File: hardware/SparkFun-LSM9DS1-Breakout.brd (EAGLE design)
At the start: 22.9 x 22.9 mm, 27 parts, among them U1 LSM9DS1

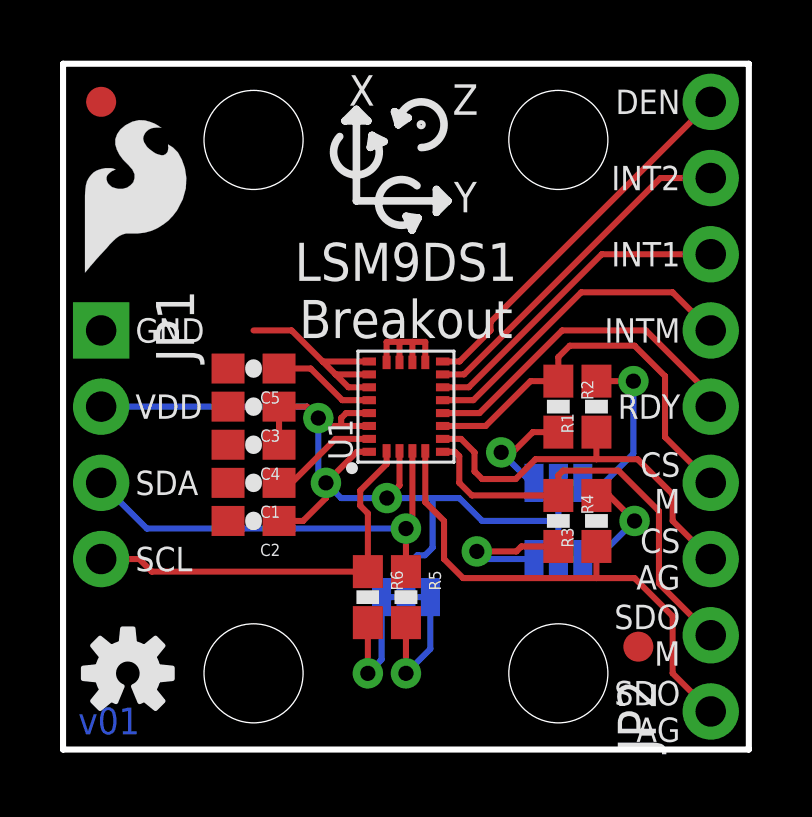
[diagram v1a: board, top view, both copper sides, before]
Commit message: Adding board mesurements, fixing some traces, labelling VCC range.
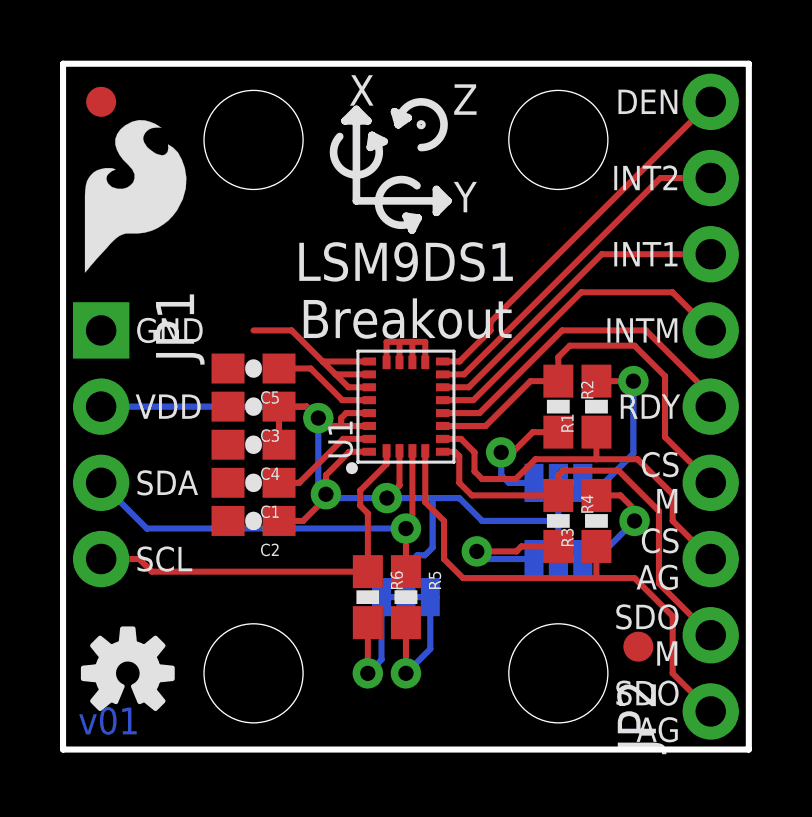
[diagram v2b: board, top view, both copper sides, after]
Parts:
- moved FRAME1 12.7 mm to (-15.2, -22.9)
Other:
- board text added: "1.9-3.6V"
- board text added: "Units in inches"
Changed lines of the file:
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@@
 <setting verticaltext="up"/>
 </settings>
-<grid distance="0.05" unitdist="inch" unit="inch" style="lines" multiple="1" display="yes" altdistance="0.005" altunitdist="inch" altunit="inch"/>
+<grid distance="0.05" unitdist="inch" unit="inch" style="lines" multiple="1" display="yes" altdistance="0.0025" altunitdist="inch" altunit="inch"/>
 <layers>
 <layer number="1" name="Top" color="4" fill="1" visible="yes" active="yes"/>
@@
 <layer number="47" name="Measures" color="7" fill="1" visible="no" active="yes"/>
 <layer number="48" name="Document" color="7" fill="1" visible="no" active="yes"/>
-<layer number="49" name="Reference" color="7" fill="1" visible="no" active="yes"/>
+<layer number="49" name="Reference" color="7" fill="1" visible="yes" active="yes"/>
 <layer number="50" name="dxf" color="7" fill="1" visible="no" active="no"/>
 <layer number="51" name="tDocu" color="6" fill="1" visible="yes" active="yes"/>
@@
 <text x="20.574" y="11.43" size="0.8128" layer="21" font="vector" ratio="15" align="center-right">RDY</text>
 <text x="2.286" y="13.97" size="0.8128" layer="22" font="vector" ratio="15" rot="MR0" align="center-right">GND</text>
-<text x="2.286" y="11.43" size="0.8128" layer="22" font="vector" ratio="15" rot="MR0" align="center-right">VDD</text>
+<text x="2.286" y="11.43" size="0.8128" layer="22" font="vector" ratio="15" rot="MR0" align="center-right">1.9-3.6V</text>
 <text x="2.286" y="8.89" size="0.8128" layer="22" font="vector" ratio="15" rot="MR0" align="center-right">SDA</text>
 <text x="2.286" y="6.35" size="0.8128" layer="22" font="vector" ratio="15" rot="MR0" align="center-right">SCL</text>
@@
 <text x="17.272" y="10.033" size="0.8128" layer="22" font="vector" ratio="15" rot="MR0" align="bottom-center">AG</text>
 <text x="9.398" y="4.699" size="0.8128" layer="22" font="vector" ratio="15" rot="MR0" align="bottom-center">I</text>
-<text x="7.366" y="4.699" size="0.8128" layer="22" font="vector" ratio="15" rot="MR0" align="bottom-center">C PU</text>
-<text x="9.017" y="5.334" size="0.635" layer="22" font="vector" ratio="15" rot="MR0" align="bottom-center">2</text>
+<text x="7.239" y="4.699" size="0.8128" layer="22" font="vector" ratio="15" rot="MR0" align="bottom-center">C PU</text>
+<text x="8.9535" y="5.2705" size="0.635" layer="22" font="vector" ratio="15" rot="MR0" align="bottom-center">2</text>
 <text x="13.0556" y="17.9324" size="0.8128" layer="22" font="vector" ratio="15" rot="MR0" align="center">SDO
 0
@@
 <wire x1="13.9954" y1="17.2974" x2="8.4836" y2="17.2974" width="0.127" layer="22"/>
 <text x="11.557" y="21.971" size="0.762" layer="22" font="vector" ratio="15" rot="MR0" align="center">2</text>
+<dimension x1="0" y1="0" x2="22.86" y2="0" x3="11.43" y3="-13.97" textsize="0.889" textratio="15" layer="47" unit="inch"/>
+<dimension x1="1.27" y1="6.35" x2="0" y2="6.35" x3="0.635" y3="-2.54" textsize="0.889" textratio="15" layer="47" unit="inch"/>
+<dimension x1="6.35" y1="2.54" x2="0" y2="2.54" x3="3.175" y3="-5.08" textsize="0.889" textratio="15" layer="47" unit="inch"/>
+<dimension x1="16.51" y1="2.54" x2="0" y2="2.54" x3="8.255" y3="-7.62" textsize="0.889" textratio="15" layer="47" unit="inch"/>
+<dimension x1="21.59" y1="1.27" x2="0" y2="1.27" x3="10.795" y3="-10.16" textsize="0.889" textratio="15" layer="47" unit="inch"/>
+<dimension x1="6.35" y1="2.54" x2="6.35" y2="0" x3="-3.81" y3="1.27" textsize="0.889" textratio="15" layer="47" unit="inch"/>
+<dimension x1="21.59" y1="1.27" x2="21.59" y2="0" x3="-1.27" y3="0.635" textsize="0.889" textratio="15" layer="47" unit="inch"/>
+<dimension x1="1.27" y1="6.35" x2="1.27" y2="0" x3="-6.35" y3="3.175" textsize="0.889" textratio="15" layer="47" unit="inch"/>
+<dimension x1="6.35" y1="20.32" x2="6.35" y2="0" x3="-11.43" y3="10.16" textsize="0.889" textratio="15" layer="47" unit="inch"/>
+<dimension x1="0" y1="22.86" x2="0" y2="0" x3="-13.97" y3="11.43" textsize="0.889" textratio="15" layer="47" unit="inch"/>
+<text x="-12.7" y="-10.16" size="0.889" layer="47" font="vector" ratio="15">Units in inches</text>
+<dimension x1="1.27" y1="8.89" x2="1.27" y2="0" x3="-8.89" y3="4.445" textsize="0.889" textratio="15" layer="47" unit="inch"/>
+<dimension x1="6.35" y1="20.32" x2="8.001" y2="20.32" x3="7.1755" y3="24.13" textsize="0.889" textratio="15" layer="47" unit="inch" precision="3"/>
 </plain>
 <attributes>
@@
 </autorouter>
 <elements>
-<element name="FRAME1" library="SparkFun-Aesthetics" package="CREATIVE_COMMONS" value="" x="-15.24" y="-10.16" smashed="yes">
+<element name="FRAME1" library="SparkFun-Aesthetics" package="CREATIVE_COMMONS" value="" x="-15.24" y="-22.86" smashed="yes">
 <attribute name="VERSION" value="v01" x="0.508" y="0.508" size="0.889" layer="16" font="vector" ratio="15"/>
-<attribute name="DESIGNER" value="Jim Lindblom" x="15.24" y="-10.16" size="1.778" layer="51" font="vector" ratio="15"/>
+<attribute name="DESIGNER" value="Jim Lindblom" x="15.24" y="-22.86" size="1.778" layer="51" font="vector" ratio="15"/>
 </element>
 <element name="U1" library="LSM9DS1_temp" package="LGA24-8X4" value="LSM9DS1" x="11.43" y="11.43" rot="R90">
@@
 <contactref element="C1" pad="1"/>
 <contactref element="U1" pad="24"/>
-<wire x1="10.205" y1="10.355" x2="9.085" y2="10.355" width="0.2032" layer="1"/>
-<wire x1="9.085" y1="10.355" x2="7.62" y2="8.89" width="0.2032" layer="1"/>
-<wire x1="7.62" y1="8.89" x2="7.2" y2="8.89" width="0.2032" layer="1"/>
+<wire x1="10.205" y1="10.355" x2="9.339" y2="10.355" width="0.2032" layer="1"/>
+<wire x1="9.339" y1="10.355" x2="7.874" y2="8.89" width="0.2032" layer="1"/>
+<wire x1="7.874" y1="8.89" x2="7.2" y2="8.89" width="0.2032" layer="1"/>
 </signal>
 <signal name="GND">
@@
 <contactref element="JP1" pad="2"/>
 <wire x1="10.205" y1="10.785" x2="9.271" y2="10.785" width="0.2032" layer="1"/>
-<via x="8.763" y="8.89" extent="1-16" drill="0.508"/>
+<via x="8.763" y="8.509" extent="1-16" drill="0.508"/>
 <wire x1="9.271" y1="10.785" x2="8.773" y2="10.785" width="0.2032" layer="1"/>
-<wire x1="10.205" y1="9.925" x2="9.798" y2="9.925" width="0.2032" layer="1"/>
-<wire x1="9.798" y1="9.925" x2="8.763" y2="8.89" width="0.2032" layer="1"/>
+<wire x1="10.205" y1="9.925" x2="9.544" y2="9.925" width="0.2032" layer="1"/>
 <via x="10.795" y="8.382" extent="1-16" drill="0.508"/>
 <wire x1="11.215" y1="9.955" x2="11.215" y2="8.802" width="0.2032" layer="1"/>
-<wire x1="10.795" y1="8.382" x2="9.271" y2="8.382" width="0.2032" layer="16"/>
-<wire x1="9.271" y1="8.382" x2="8.763" y2="8.89" width="0.2032" layer="16"/>
+<wire x1="10.795" y1="8.382" x2="8.89" y2="8.382" width="0.2032" layer="16"/>
+<wire x1="8.89" y1="8.382" x2="8.763" y2="8.509" width="0.2032" layer="16"/>
 <wire x1="11.215" y1="8.802" x2="10.795" y2="8.382" width="0.2032" layer="1"/>
 <wire x1="13.208" y1="8.382" x2="12.319" y2="8.382" width="0.2032" layer="16"/>
@@
 <wire x1="7.2" y1="7.62" x2="8.001" y2="7.62" width="0.2032" layer="1"/>
 <wire x1="8.001" y1="7.62" x2="8.763" y2="8.382" width="0.2032" layer="1"/>
-<wire x1="8.763" y1="8.382" x2="8.763" y2="8.89" width="0.2032" layer="1"/>
+<wire x1="8.763" y1="8.382" x2="8.763" y2="8.4455" width="0.2032" layer="1"/>
+<wire x1="8.763" y1="8.4455" x2="8.763" y2="8.509" width="0.2032" layer="1"/>
 <wire x1="8.128" y1="11.43" x2="8.509" y2="11.049" width="0.2032" layer="16"/>
-<wire x1="8.763" y1="8.89" x2="8.509" y2="9.144" width="0.2032" layer="16"/>
-<wire x1="8.509" y1="9.144" x2="8.509" y2="11.049" width="0.2032" layer="16"/>
+<wire x1="8.763" y1="8.509" x2="8.509" y2="8.763" width="0.2032" layer="16"/>
+<wire x1="8.509" y1="8.763" x2="8.509" y2="11.049" width="0.2032" layer="16"/>
 <wire x1="10.205" y1="11.215" x2="9.437" y2="11.215" width="0.2032" layer="1"/>
 <wire x1="9.437" y1="11.215" x2="9.271" y2="11.049" width="0.2032" layer="1"/>
@@
 <wire x1="8.128" y1="11.43" x2="8.509" y2="11.049" width="0.2032" layer="1"/>
 <wire x1="1.27" y1="11.43" x2="8.128" y2="11.43" width="0.2032" layer="16"/>
+<wire x1="9.544" y1="9.925" x2="8.763" y2="9.144" width="0.2032" layer="1"/>
+<wire x1="8.763" y1="9.144" x2="8.763" y2="8.509" width="0.2032" layer="1"/>
 </signal>
 <signal name="SDA">
@@
 <wire x1="14.986" y1="9.906" x2="14.605" y2="9.906" width="0.2032" layer="1"/>
 <via x="14.605" y="9.906" extent="1-16" drill="0.508"/>
-<wire x1="15.6972" y1="8.89" x2="15.621" y2="8.89" width="0.2032" layer="16"/>
-<wire x1="15.621" y1="8.89" x2="14.605" y2="9.906" width="0.2032" layer="16"/>
+<wire x1="15.6972" y1="8.89" x2="14.859" y2="8.89" width="0.2032" layer="16"/>
+<wire x1="14.859" y1="8.89" x2="14.605" y2="9.144" width="0.2032" layer="16"/>
+<wire x1="14.605" y1="9.144" x2="14.605" y2="9.906" width="0.2032" layer="16"/>
 </signal>
 <signal name="SDO_A/G_PU">
 <contactref element="R3" pad="2"/>
 <contactref element="SJ2" pad="3"/>
-<wire x1="17.78" y1="8.47" x2="18.2" y2="8.47" width="0.2032" layer="1"/>
-<wire x1="18.2" y1="8.47" x2="19.05" y2="7.62" width="0.2032" layer="1"/>
+<wire x1="17.78" y1="8.47" x2="18.581" y2="8.47" width="0.2032" layer="1"/>
 <via x="19.05" y="7.62" extent="1-16" drill="0.508"/>
 <wire x1="17.3228" y1="6.35" x2="17.78" y2="6.35" width="0.2032" layer="16"/>
 <wire x1="17.78" y1="6.35" x2="19.05" y2="7.62" width="0.2032" layer="16"/>
+<wire x1="19.05" y1="7.62" x2="19.05" y2="8.001" width="0.2032" layer="1"/>
+<wire x1="19.05" y1="8.001" x2="18.581" y2="8.47" width="0.2032" layer="1"/>
 </signal>
 <signal name="SDO_M_PU">

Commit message: Re-arranging some silk. Updating board to v10.
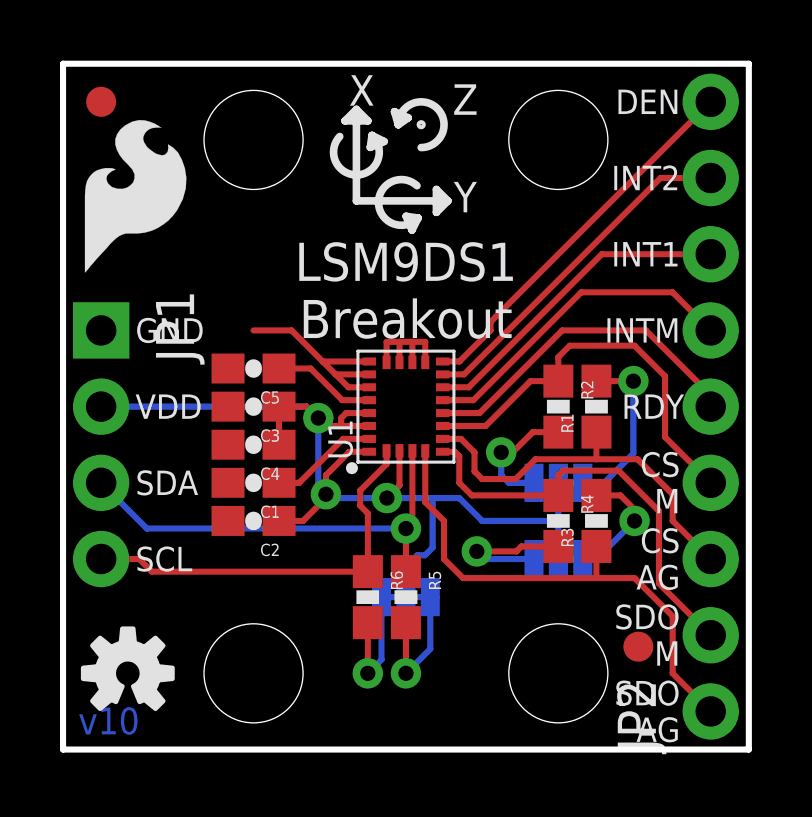
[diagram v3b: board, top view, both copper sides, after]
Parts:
- moved LOGO1 0.40 mm to (17.4, 12.4)
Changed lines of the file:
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@@
 <setting verticaltext="up"/>
 </settings>
-<grid distance="0.05" unitdist="inch" unit="inch" style="lines" multiple="1" display="yes" altdistance="0.0025" altunitdist="inch" altunit="inch"/>
+<grid distance="0.05" unitdist="inch" unit="inch" style="lines" multiple="1" display="yes" altdistance="0.005" altunitdist="inch" altunit="inch"/>
 <layers>
 <layer number="1" name="Top" color="4" fill="1" visible="yes" active="yes"/>
@@
 <wire x1="10.24095" y1="20.072690625" x2="10.7017125" y2="20.267678125" width="0.254" layer="21"/>
 <wire x1="10.7017125" y1="20.267678125" x2="10.299653125" y2="20.469984375" width="0.254" layer="21"/>
-<text x="20.574" y="11.43" size="0.8128" layer="21" font="vector" ratio="15" align="center-right">RDY</text>
+<text x="20.701" y="11.43" size="0.8128" layer="21" font="vector" ratio="15" align="center-right">RDY</text>
 <text x="2.286" y="13.97" size="0.8128" layer="22" font="vector" ratio="15" rot="MR0" align="center-right">GND</text>
 <text x="2.286" y="11.43" size="0.8128" layer="22" font="vector" ratio="15" rot="MR0" align="center-right">1.9-3.6V</text>
@@
 AG</text>
 <text x="20.447" y="11.43" size="0.8128" layer="22" font="vector" ratio="15" rot="MR0" align="center-left">RDY</text>
-<text x="15.24" y="13.335" size="0.889" layer="22" font="vector" ratio="15" rot="MR0" align="top-left">LSM9DS1
+<text x="11.43" y="13.462" size="0.889" layer="22" font="vector" ratio="15" rot="MR0" align="top-center">LSM9DS1
 Breakout</text>
 <text x="14.859" y="8.89" size="0.8128" layer="22" font="vector" ratio="15" rot="MR270" align="bottom-center">CS</text>
 <text x="14.859" y="6.35" size="0.8128" layer="22" font="vector" ratio="15" rot="MR270" align="bottom-center">SDO</text>
-<text x="15.494" y="10.033" size="0.8128" layer="22" font="vector" ratio="15" rot="MR0" align="bottom-center">M</text>
-<text x="17.272" y="10.033" size="0.8128" layer="22" font="vector" ratio="15" rot="MR0" align="bottom-center">AG</text>
-<text x="9.398" y="4.699" size="0.8128" layer="22" font="vector" ratio="15" rot="MR0" align="bottom-center">I</text>
-<text x="7.239" y="4.699" size="0.8128" layer="22" font="vector" ratio="15" rot="MR0" align="bottom-center">C PU</text>
-<text x="8.9535" y="5.2705" size="0.635" layer="22" font="vector" ratio="15" rot="MR0" align="bottom-center">2</text>
+<text x="15.621" y="10.033" size="0.8128" layer="22" font="vector" ratio="15" rot="MR0" align="bottom-center">M</text>
+<text x="17.399" y="10.033" size="0.8128" layer="22" font="vector" ratio="15" rot="MR0" align="bottom-center">AG</text>
+<text x="12.954" y="2.667" size="0.8128" layer="22" font="vector" ratio="15" rot="MR0" align="bottom-center">I</text>
+<text x="10.795" y="2.667" size="0.8128" layer="22" font="vector" ratio="15" rot="MR0" align="bottom-center">C PU</text>
+<text x="12.5095" y="3.2385" size="0.635" layer="22" font="vector" ratio="15" rot="MR0" align="bottom-center">2</text>
 <text x="13.0556" y="17.9324" size="0.8128" layer="22" font="vector" ratio="15" rot="MR0" align="center">SDO
 0
@@
 <dimension x1="1.27" y1="8.89" x2="1.27" y2="0" x3="-8.89" y3="4.445" textsize="0.889" textratio="15" layer="47" unit="inch"/>
 <dimension x1="6.35" y1="20.32" x2="8.001" y2="20.32" x3="7.1755" y3="24.13" textsize="0.889" textratio="15" layer="47" unit="inch" precision="3"/>
+<wire x1="16.51" y1="10.922" x2="16.51" y2="9.906" width="0.1524" layer="22"/>
+<wire x1="16.51" y1="7.874" x2="16.51" y2="7.366" width="0.1524" layer="22"/>
 </plain>
 <attributes>
@@
 <elements>
 <element name="FRAME1" library="SparkFun-Aesthetics" package="CREATIVE_COMMONS" value="" x="-15.24" y="-22.86" smashed="yes">
-<attribute name="VERSION" value="v01" x="0.508" y="0.508" size="0.889" layer="16" font="vector" ratio="15"/>
+<attribute name="VERSION" value="v10" x="0.508" y="0.508" size="0.889" layer="16" font="vector" ratio="15"/>
 <attribute name="DESIGNER" value="Jim Lindblom" x="15.24" y="-22.86" size="1.778" layer="51" font="vector" ratio="15"/>
 </element>
@@
 <element name="SJ3" library="SparkFun-Passives" package="PAD-JUMPER-3-3OF3_NC_BY_TRACE_YES_SILK_FULL_BOX" value="" x="11.43" y="5.08" rot="MR0"/>
 <element name="JP2" library="SparkFun-Connectors" package="1X09_NO_SILK" value="M09NO_SILK" x="21.59" y="1.27" rot="R90"/>
-<element name="LOGO1" library="SparkFun-Aesthetics" package="SFE_LOGO_NAME_.1" value="SFE_LOGO_NAME.1_INCH" x="17.78" y="12.319" rot="MR0"/>
+<element name="LOGO1" library="SparkFun-Aesthetics" package="SFE_LOGO_NAME_.1" value="SFE_LOGO_NAME.1_INCH" x="17.399" y="12.446" rot="MR0"/>
 <element name="LOGO2" library="SparkFun-Aesthetics" package="SFE_LOGO_FLAME_.2" value="SFE_LOGO_FLAME.2_INCH" x="0.381" y="15.621"/>
 <element name="LOGO3" library="SparkFun-Aesthetics" package="OSHW-LOGO-S" value="OSHW-LOGOS" x="2.159" y="2.54"/>
